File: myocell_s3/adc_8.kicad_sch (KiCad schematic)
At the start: 45 parts, among them U1 OPA340NA, U2 ADS1298xPAG, U3 OPA340NA

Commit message: working on schematic
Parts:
- removed R14, R30: 0, Resistor_SMD:R_0805_2012Metric_Pad1.20x1.40mm_HandSolder, symbol Device:R_US
- removed R15, R31: TBD, Resistor_SMD:R_0805_2012Metric_Pad1.20x1.40mm_HandSolder, symbol Device:R_US
- removed U1, U3: OPA340NA, Package_TO_SOT_SMD:SOT-23-5, symbol Amplifier_Operational:OPA340NA
- added C31, C32, C33, C42, C43, C44, C45, C46, C47, C48, C49, C50, C51, C52, C53, C54: 47pF, Capacitor_SMD:C_0805_2012Metric_Pad1.18x1.45mm_HandSolder, symbol Device:C
- added R19, R35, R36, R43, R47: 22k, Resistor_SMD:R_0805_2012Metric_Pad1.20x1.40mm_HandSolder, symbol Device:R_US
- added R20, R21, R22, R23, R24, R33, R34, R37, R38, R39, R40, R41, R42, R44, R45, R46, R48, R49, R50: 10k, Resistor_SMD:R_0805_2012Metric_Pad1.20x1.40mm_HandSolder, symbol Device:R_US
- C1, C2, C3, C4, C5, C6, C7, C8: value 22uF -> 47pF
- C21: value 0.1uF -> ~
- C9: value 0.1uF -> 47pF
- R1: value 5k -> 22k
- R2: value 5k -> 10k
- R3, R7, R8: value 10k -> 22k
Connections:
- net 3.3VA: now also R6.2, R22.2, R33.2, R34.2, R41.2, R42.2, R46.2, R50.2
- net GNDA: now also C1.2, C2.2, C21.1, C4.2, C5.2, C6.2, C8.2, R5.2, C31.2, C32.2, C43.2, C44.2, C45.2, C46.2, C49.2, C50.2, C52.2, C53.2, R21.2, R23.2, R24.2, R39.2, R40.2, R45.2, R49.2; no longer C21.2, R2.2
- net IN1N: now also R3.1; no longer C5.2
- net IN1P: now also R19.1; no longer C1.2
- net IN2N: now also R8.1; no longer C6.2
- net IN2P: now also R7.1; no longer C2.2
- net IN3N: now also R36.1; no longer C7.2
- net IN3P: now also R35.1; no longer C3.2
- net IN4N: now also R47.1; no longer C8.2
- net IN4P: now also R43.1; no longer C4.2
- net at C16.2, R13.1, U2.63 (RLDOUT): now also R1.1
- net at C10.2, C11.2, U2.24 (VREFP): no longer R1.1
- net at R1.2, R2.1: now also C9.2
- removed net +3.3VA: C21.1, C9.2
- removed net V_0: R10.1, R3.1, R4.1, R5.1, R6.1, R7.1, R8.1, R9.1
- new net: C32.1, C42.1, R10.2
- new net: C2.1, C3.1, R20.2
- new net: C3.2, R21.1, R22.1, U2.16 (IN1P)
- new net: C31.1, C33.1, R9.2
- new net: C7.2, R5.1, R6.1, U2.15 (IN1N)
- new net: C53.1, C54.1, R48.2
- new net: C54.2, R49.1, R50.1, U2.9 (IN4N)
- new net: C42.2, R24.1, R34.1, U2.13 (IN2N)
- new net: C44.1, R36.2, R38.1
- new net: C52.1, R47.2, R48.1
- new net: C51.2, R45.1, R46.1, U2.10 (IN4P)
- new net: C48.2, R40.1, R42.1, U2.11 (IN3N)
- new net: C47.2, R39.1, R41.1, U2.12 (IN3P)
- new net: C33.2, R23.1, R33.1, U2.14 (IN2P)
- new net: C8.1, R10.1, R8.2
- new net: C6.1, C7.1, R4.2
- new net: C1.1, R19.2, R20.1
- new net: C45.1, C47.1, R37.2
- new net: C43.1, R35.2, R37.1
- new net: C4.1, R3.2, R4.1
- new net: C50.1, C51.1, R44.2
- new net: C49.1, R43.2, R44.1
- new net: C5.1, R7.2, R9.1
- new net: C46.1, C48.1, R38.2
- new net RLD: C21.2, R2.2
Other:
- note added: "When using the internal voltage reference, connect VREFN to AVSS"
- note added: "https://static.chipdip.ru/lib/687/DOC011687749.pdf Analog filter ADS1298RECG-FE ECG Front-End Performance Demonstration Kit"
- note removed: "1.2v"
- note removed: "2.4v"
- note removed: "Zero level to ADC"
- moved on the sheet: C1, C10, C11, C12, C13, C14, C15, C16, C17, C18, C19, C20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

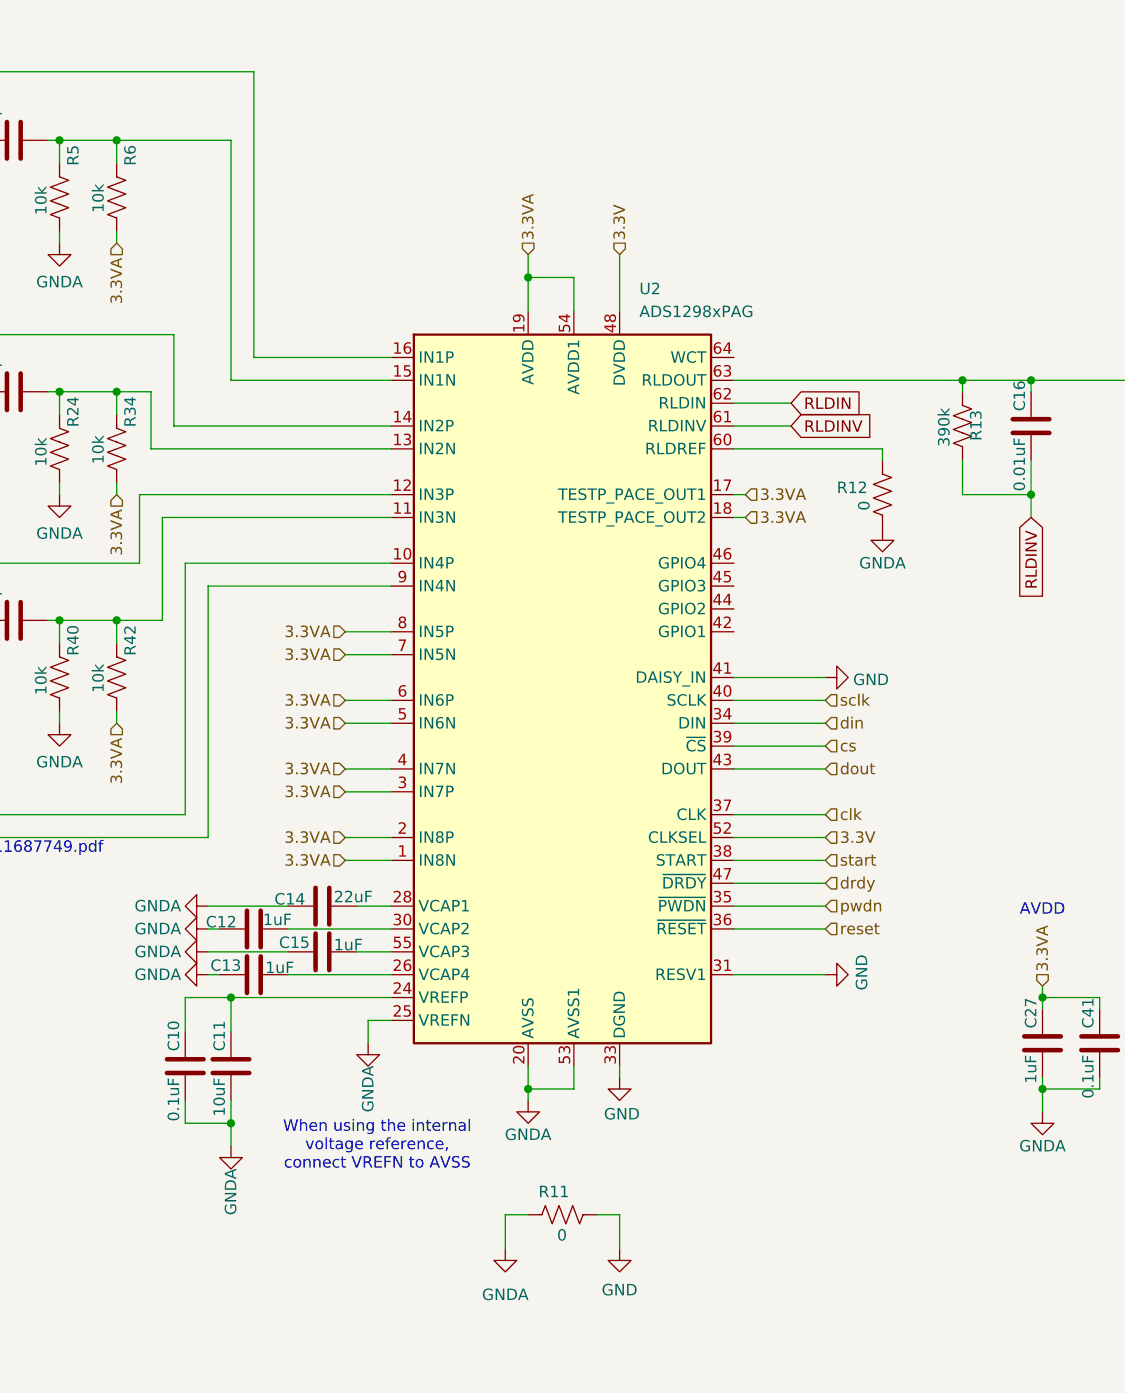
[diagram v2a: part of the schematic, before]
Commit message: RLDINV still unconnected
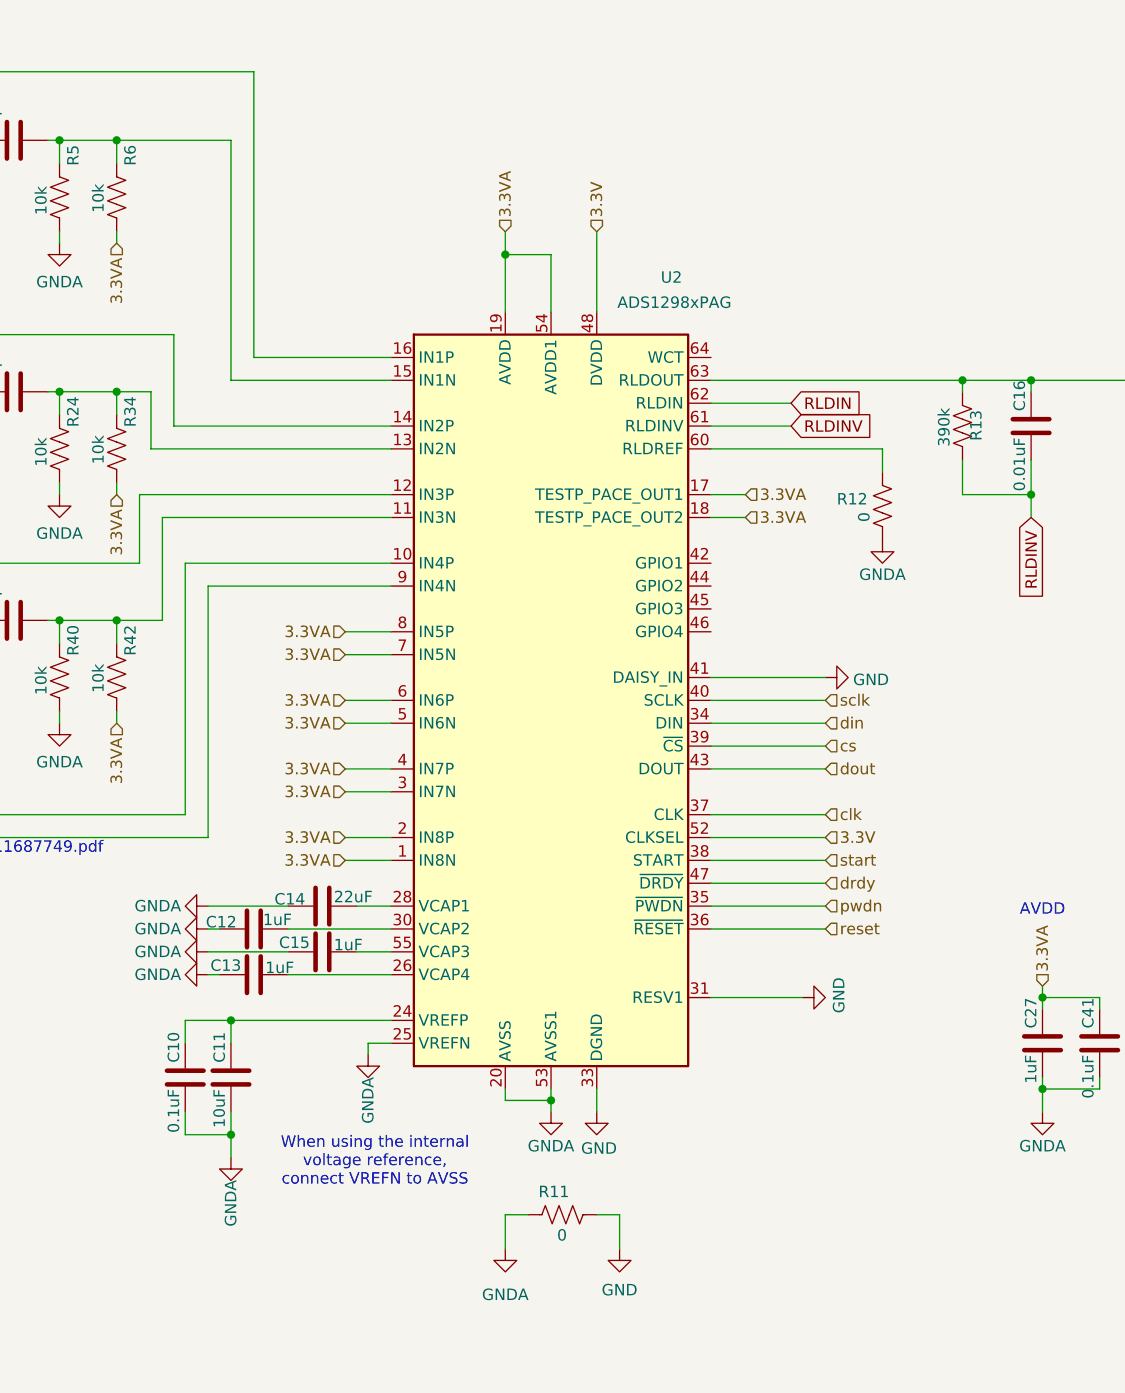
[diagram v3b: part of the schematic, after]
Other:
- moved on the sheet: C10, C11, R12, U2

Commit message: schematic and footprints done
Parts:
- added R17: 0, Resistor_SMD:R_0805_2012Metric_Pad1.20x1.40mm_HandSolder, symbol Device:R_US
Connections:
- net at C16.2, R1.1, R13.1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: now also R17.1
- net RLDIN: no longer names the net of U2.62 (RLDIN)
- net RLDIN: now also R17.2
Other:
- moved on the sheet: C16, R13
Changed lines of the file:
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@@
 	)
 	(junction
-		(at 205.74 53.34)
+		(at 213.36 53.34)
 		(diameter 0)
 		(color 0 0 0 0)
@@
 	)
 	(junction
-		(at 213.36 53.34)
+		(at 220.98 53.34)
 		(diameter 0)
 		(color 0 0 0 0)
 	)
 	(junction
-		(at 213.36 66.04)
+		(at 201.93 53.34)
+		(diameter 0)
+		(color 0 0 0 0)
+	)
+	(junction
+		(at 220.98 66.04)
 		(diameter 0)
 		(color 0 0 0 0)
@@
 	(wire
 		(pts
-			(xy 205.74 66.04) (xy 205.74 62.23)
+			(xy 213.36 66.04) (xy 213.36 62.23)
 		)
 		(stroke
@@
 	(wire
 		(pts
-			(xy 213.36 66.04) (xy 213.36 68.58)
+			(xy 220.98 66.04) (xy 220.98 68.58)
 		)
 		(stroke
@@
 	(wire
 		(pts
-			(xy 213.36 53.34) (xy 226.06 53.34)
+			(xy 220.98 53.34) (xy 226.06 53.34)
 		)
 		(stroke
@@
 	(wire
 		(pts
-			(xy 213.36 62.23) (xy 213.36 66.04)
+			(xy 220.98 62.23) (xy 220.98 66.04)
 		)
 		(stroke
@@
 	(wire
 		(pts
-			(xy 177.8 55.88) (xy 186.69 55.88)
+			(xy 177.8 55.88) (xy 184.15 55.88)
 		)
 		(stroke
@@
 	(wire
 		(pts
+			(xy 201.93 53.34) (xy 213.36 53.34)
+		)
+		(stroke
+			(width 0)
+			(type default)
+		)
+	)
+	(wire
+		(pts
 			(xy 31.75 138.43) (xy 31.75 137.16)
 		)
@@
 	(wire
 		(pts
-			(xy 177.8 53.34) (xy 205.74 53.34)
+			(xy 177.8 53.34) (xy 201.93 53.34)
 		)
 		(stroke
@@
 	(wire
 		(pts
-			(xy 205.74 53.34) (xy 213.36 53.34)
+			(xy 213.36 53.34) (xy 220.98 53.34)
 		)
 		(stroke
@@
 	(wire
 		(pts
-			(xy 177.8 58.42) (xy 186.69 58.42)
+			(xy 177.8 58.42) (xy 189.23 58.42)
 		)
 		(stroke
@@
 	(wire
 		(pts
+			(xy 201.93 55.88) (xy 201.93 53.34)
+		)
+		(stroke
+			(width 0)
+			(type default)
+		)
+	)
+	(wire
+		(pts
 			(xy 59.69 83.82) (xy 59.69 85.09)
 		)
@@
 	(wire
 		(pts
-			(xy 205.74 53.34) (xy 205.74 54.61)
+			(xy 213.36 53.34) (xy 213.36 54.61)
 		)
 		(stroke
@@
 	(wire
 		(pts
-			(xy 213.36 53.34) (xy 213.36 54.61)
+			(xy 220.98 53.34) (xy 220.98 54.61)
 		)
 		(stroke
@@
 	(wire
 		(pts
+			(xy 191.77 55.88) (xy 201.93 55.88)
+		)
+		(stroke
+			(width 0)
+			(type default)
+		)
+	)
+	(wire
+		(pts
 			(xy 270.51 121.92) (xy 264.16 121.92)
 		)
@@
 	(wire
 		(pts
-			(xy 213.36 66.04) (xy 205.74 66.04)
+			(xy 220.98 66.04) (xy 213.36 66.04)
 		)
 		(stroke
@@
 	(global_label "RLDINV"
 		(shape input)
-		(at 213.36 68.58 270)
+		(at 220.98 68.58 270)
 		(fields_autoplaced yes)
 		(effects
@@
 		)
 		(property "Intersheetrefs" "${INTERSHEET_REFS}"
-			(at 213.36 78.1572 90)
+			(at 220.98 78.1572 90)
 			(effects
 				(font
@@
 	(global_label "RLDINV"
 		(shape input)
-		(at 186.69 58.42 0)
-		(fields_autoplaced yes)
-		(effects
-			(font
-				(size 1.27 1.27)
-			)
-			(justify left)
-		)
-		(property "Intersheetrefs" "${INTERSHEET_REFS}"
-			(at 196.2672 58.42 0)
-			(effects
-				(font
-					(size 1.27 1.27)
-				)
-				(justify left)
-				(hide yes)
-			)
-		)
-	)
-	(global_label "RLDIN"
-		(shape input)
-		(at 186.69 55.88 0)
+		(at 189.23 58.42 0)
 		(fields_autoplaced yes)
 		(effects
@@
 		)
 		(property "Intersheetrefs" "${INTERSHEET_REFS}"
-			(at 195.1786 55.88 0)
+			(at 198.8072 58.42 0)
 			(effects
 				(font
@@
 	(symbol
 		(lib_id "Device:C")
-		(at 213.36 58.42 180)
+		(at 220.98 58.42 180)
 		(unit 1)
 		(exclude_from_sim no)
@@
 		(dnp no)
 		(property "Reference" "C16"
-			(at 212.09 53.34 90)
+			(at 219.71 53.34 90)
 			(effects
 				(font
@@
 		)
 		(property "Value" "0.01uF"
-			(at 212.09 59.69 90)
+			(at 219.71 59.69 90)
 			(effects
 				(font
@@
 		)
 		(property "Footprint" "Capacitor_SMD:C_0805_2012Metric_Pad1.18x1.45mm_HandSolder"
-			(at 212.3948 54.61 0)
+			(at 220.0148 54.61 0)
 			(effects
 				(font
@@
 		)
 		(property "Datasheet" "~"
-			(at 213.36 58.42 0)
+			(at 220.98 58.42 0)
 			(effects
 				(font
@@
 		)
 		(property "Description" "Unpolarized capacitor"
-			(at 213.36 58.42 0)
+			(at 220.98 58.42 0)
 			(effects
 				(font
@@
 	(symbol
 		(lib_id "Device:R_US")
-		(at 205.74 58.42 0)
+		(at 213.36 58.42 0)
 		(unit 1)
 		(exclude_from_sim no)
@@
 		(dnp no)
 		(property "Reference" "R13"
-			(at 207.264 56.642 90)
+			(at 214.884 56.642 90)
 			(effects
 				(font
@@
 		)
 		(property "Value" "390k"
-			(at 203.708 56.388 90)
+			(at 211.328 56.388 90)
 			(effects
 				(font
@@
 		)
 		(property "Footprint" "Resistor_SMD:R_0805_2012Metric_Pad1.20x1.40mm_HandSolder"
-			(at 206.756 58.674 90)
+			(at 214.376 58.674 90)
 			(effects
 				(font
@@
 		)
 		(property "Datasheet" "~"
-			(at 205.74 58.42 0)
+			(at 213.36 58.42 0)
 			(effects
 				(font
@@
 		)
 		(property "Description" "Resistor, US symbol"
-			(at 205.74 58.42 0)
+			(at 213.36 58.42 0)
 			(effects
 				(font
@@
 					(unit 1)
 				)
+			)
+		)
+	)
+	(symbol
+		(lib_id "Device:R_US")
+		(at 187.96 55.88 270)
+		(unit 1)
+		(exclude_from_sim no)
+		(in_bom yes)
+		(on_board yes)
+		(dnp no)
+		(property "Reference" "R17"
+			(at 189.484 52.07 90)
+			(effects
+				(font
+					(size 1.27 1.27)
+				)
+				(justify right)
+			)
+		)
+		(property "Value" "0"
+			(at 191.008 54.61 90)
+			(effects
+				(font
+					(size 1.27 1.27)
+				)
+				(justify right)
+			)
+		)
+		(property "Footprint" "Resistor_SMD:R_0805_2012Metric_Pad1.20x1.40mm_HandSolder"
+			(at 187.706 56.896 90)
+			(effects
+				(font
+					(size 1.27 1.27)
+				)
+				(hide yes)
+			)
+		)
+		(property "Datasheet" "~"
+			(at 187.96 55.88 0)
+			(effects
+				(font
+					(size 1.27 1.27)
+				)
+				(hide yes)
+			)
+		)
+		(property "Description" "Resistor, US symbol"
+			(at 187.96 55.88 0)
+			(effects
+				(font
+					(size 1.27 1.27)
+				)
+				(hide yes)
+			)
+		)
+		(pin "1"
+		)
+		(pin "2"
+		)
+		(instances
+			(project "myocell_s3"
+				(path "/871ff10b-bde5-471c-b91a-de58aa271388/c595076a-24ce-4f55-8e02-687765014fdd"
+					(reference "R17")
+					(unit 1)
+				)

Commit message: working on parts placement
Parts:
- removed C31, C32, C33, C42, C43, C44, C45, C46, C47, C48, C49, C50, C51, C52, C53, C54: 47pF, Capacitor_SMD:C_0805_2012Metric_Pad1.18x1.45mm_HandSolder, symbol Device:C
- removed R34, R37, R38, R39, R40, R41, R42, R44, R45, R46, R48, R49, R50: 10k, Resistor_SMD:R_0805_2012Metric_Pad1.20x1.40mm_HandSolder, symbol Device:R_US
- removed R35, R36, R43, R47: 22k, Resistor_SMD:R_0805_2012Metric_Pad1.20x1.40mm_HandSolder, symbol Device:R_US
- added C28, C30: 2.2uF, Capacitor_SMD:C_0805_2012Metric_Pad1.18x1.45mm_HandSolder, symbol Device:C
- added R18: 5.1k, Resistor_SMD:R_0805_2012Metric_Pad1.20x1.40mm_HandSolder, symbol Device:R_US
- C1, C4: value 47pF -> 33nF
- C2, C3: value 47pF -> 2.2uF
- C5, C6, C7, C8: value 47pF -> 22nF
- R19, R7: value 22k -> 5.1k
- R3, R8: value 22k -> 10k
- R6: value 10k -> 5.1k
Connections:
- net 3.3VA: now also R3.2, R33.1, R4.1; no longer R33.2, R6.2
- net GNDA: now also C6.1, C7.2, C8.1, R10.2, R23.1, R5.1; no longer C1.2, C2.2, C4.2, C6.2, C8.2, R21.2, R23.2, R5.2
- net IN3N: now also U2.11 (IN3N)
- net IN3P: now also U2.12 (IN3P)
- net IN4N: now also U2.9 (IN4N)
- net IN4P: now also U2.10 (IN4P)
- net at R9.2: now also C3.1
- net at R24.1, U2.13 (IN2N): now also R33.2, C30.2
- net at C1.1, R20.1: now also C7.1, R18.2; no longer R19.2
- net at R7.2, R9.1: now also C4.2, C6.2; no longer C5.1
- net IN1N: no longer names the net of R3.1
- net IN1N: now also C2.2, R5.2, U2.16 (IN1P)
- net IN1P renamed IN2NF
- net IN2N: no longer names the net of R8.1
- net IN2N: now also C4.1, C5.1, R6.2
- net IN2P renamed IN1NF
- new net: C3.2, R10.1, R4.2, U2.15 (IN1N)
- new net: C28.2, R22.1, R23.2, U2.14 (IN2P)
- new net: C2.1, R8.2
- new net: C28.1, R20.2
- new net: C1.2, C8.2, R19.2, R21.1
- new net: C30.1, R21.2
- new net IN1PF: R6.1
- new net IN2PF: R18.1
